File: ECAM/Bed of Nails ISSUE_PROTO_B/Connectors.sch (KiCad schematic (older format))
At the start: 3 parts, among them J1 ERF8-020-X

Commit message: saving out files
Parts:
- gave numbers to parts that had none: 1
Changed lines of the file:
@@
 EGSE Connector
 $Comp
-L TFT_connectors:MTSW-X20 J?
+L TFT_connectors:MTSW-X20 J2
 U 1 1 60BC0133
 P 5200 1650
-F 0 "J?" H 5383 2325 50  0000 C CNN
+F 0 "J2" H 5383 2325 50  0000 C CNN
 F 1 "MTSW-X20" H 5383 2234 50  0000 C CNN
 F 2 "TFT_connectors:MSTW-120-08-D-160-RA" H 5250 2300 50  0001 C CNN
@@
 $EndComp
 $Comp
-L TFT_connectors:MTSW-X20 J?
+L TFT_connectors:MTSW-X20 J2
 U 2 1 60BC2BFD
 P 6500 1650
-F 0 "J?" H 6683 2325 50  0000 C CNN
+F 0 "J2" H 6683 2325 50  0000 C CNN
 F 1 "MTSW-X20" H 6683 2234 50  0000 C CNN
 F 2 "TFT_connectors:MSTW-120-08-D-160-RA" H 6550 2300 50  0001 C CNN
@@
 ADS_nRST
 $Comp
-L power:GND #PWR?
+L power:GND #PWR0101
 U 1 1 60BEA586
 P 6950 3200
-F 0 "#PWR?" H 6950 2950 50  0001 C CNN
+F 0 "#PWR0101" H 6950 2950 50  0001 C CNN
 F 1 "GND" H 6955 3027 50  0000 C CNN
 F 2 "" H 6950 3200 50  0001 C CNN
@@
 Connection ~ 6950 1500
 $Comp
-L TFT_power:OBC_3V3 #PWR?
+L TFT_power:OBC_3V3 #PWR0102
 U 1 1 60C131C5
 P 5800 1150
-F 0 "#PWR?" H 5800 1000 50  0001 C CNN
+F 0 "#PWR0102" H 5800 1000 50  0001 C CNN
 F 1 "OBC_3V3" H 5815 1323 50  0000 C CNN
 F 2 "" H 5800 1150 50  0001 C CNN
@@
 	5550 2100 5900 2100
 $Comp
-L power:GND #PWR?
+L power:GND #PWR0103
 U 1 1 60C29AE7
 P 5700 3200
-F 0 "#PWR?" H 5700 2950 50  0001 C CNN
+F 0 "#PWR0103" H 5700 2950 50  0001 C CNN
 F 1 "GND" H 5705 3027 50  0000 C CNN
 F 2 "" H 5700 3200 50  0001 C CNN

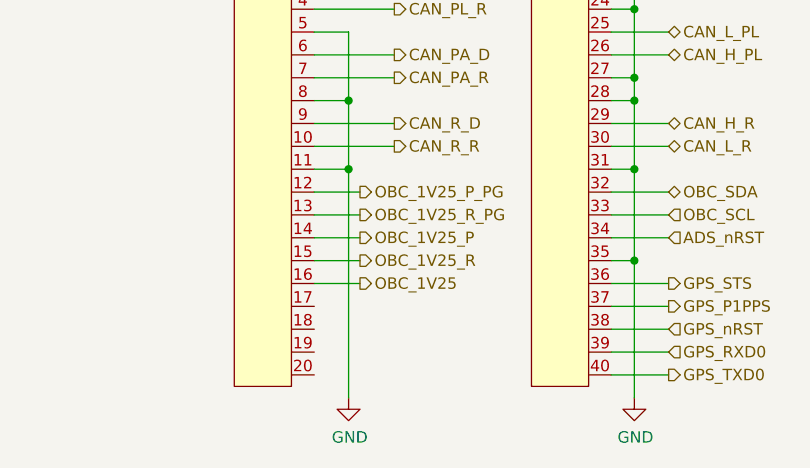
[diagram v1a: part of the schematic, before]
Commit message: updated title blocks and testpoint/connector passthroughs
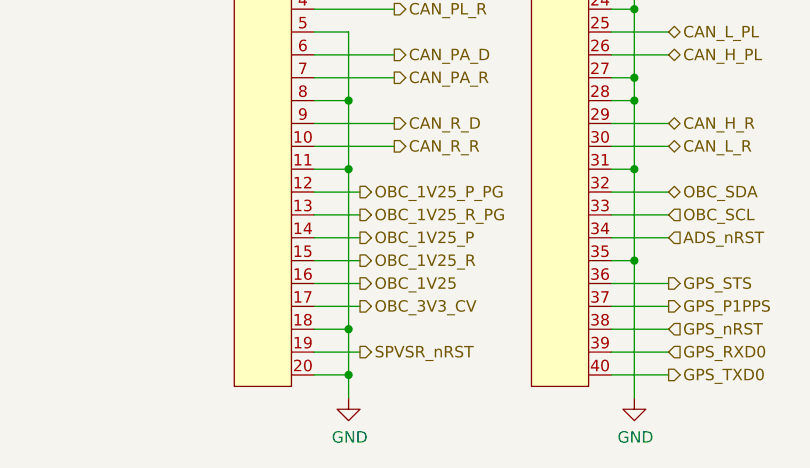
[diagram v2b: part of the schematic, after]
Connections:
- net GND: now also J2.18, J2.20
- net OBC_3V3_CV: now reaches J2.17
- net SPVSR_nRST: now reaches J2.19
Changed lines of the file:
@@
 encoding utf-8
 Sheet 2 4
-Title "Singularity OBC - Connectors"
-Date "2021-05-24"
-Rev "PROTO_B_v01"
+Title "Singularity EGSE - Connectors"
+Date "2021-06-05"
+Rev "PROTO_B_v02"
 Comp "The Flame Trench"
 Comment1 "Drawn by:  Ben Cartwright"
@@
 $EndComp
 Wire Wire Line
-	5700 3200 5700 2200
+	5700 3200 5700 3100
 Wire Wire Line
 	5700 1600 5550 1600
@@
 Wire Wire Line
 	5700 2200 5700 1900
+Text HLabel 5750 2800 2    50   Output ~ 0
+OBC_3V3_CV
+Wire Wire Line
+	5750 2800 5550 2800
+Text HLabel 5750 3000 2    50   Output ~ 0
+SPVSR_nRST
+Wire Wire Line
+	5750 3000 5550 3000
+Wire Wire Line
+	5700 2900 5550 2900
+Connection ~ 5700 2900
+Wire Wire Line
+	5700 2900 5700 2200
+Wire Wire Line
+	5700 3100 5550 3100
+Connection ~ 5700 3100
+Wire Wire Line
+	5700 3100 5700 2900
 $EndSCHEMATC
